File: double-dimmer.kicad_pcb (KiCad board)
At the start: 2 copper layers, 91.4 x 56.6 mm, 5 parts, among them J1 Netzspannung, J2 Screw_Terminal_01x05, J3 Conn_01x04

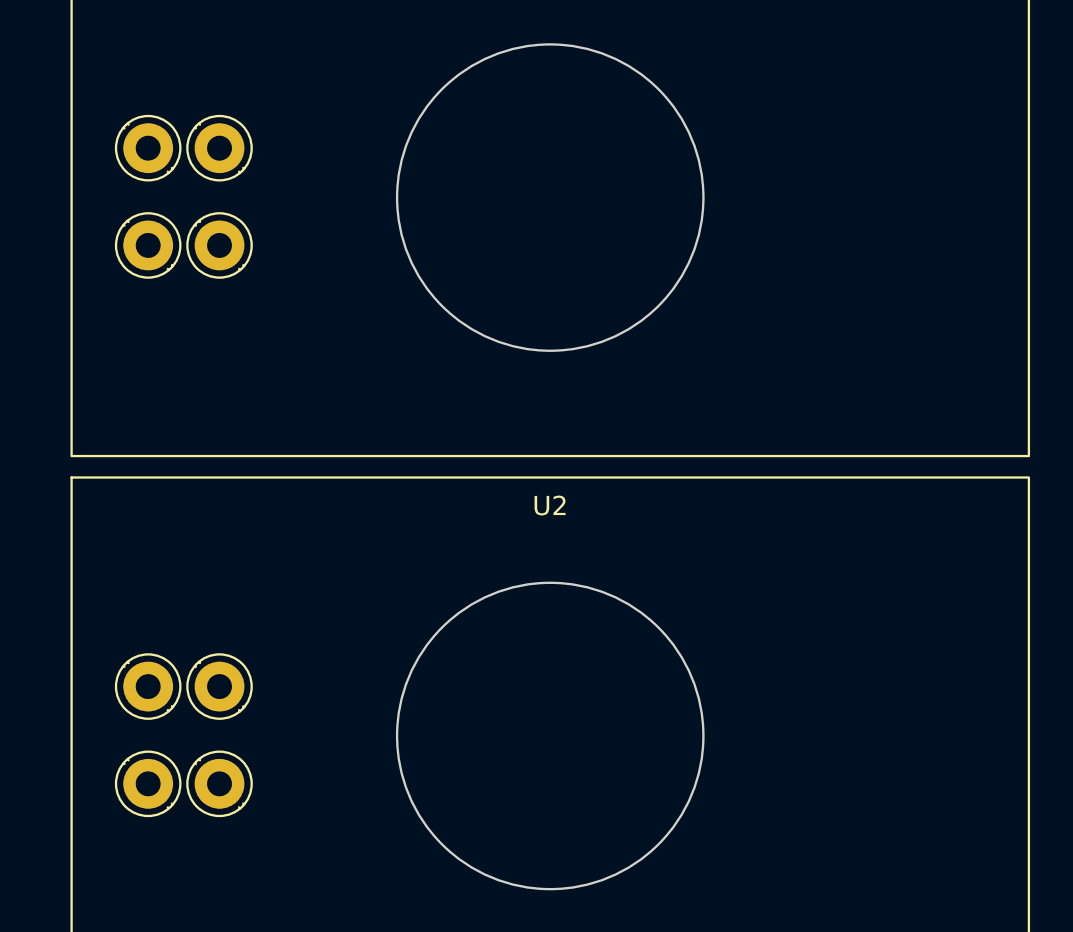
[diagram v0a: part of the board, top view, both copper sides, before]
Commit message: Update dimmer footprint and add fuse and a switch
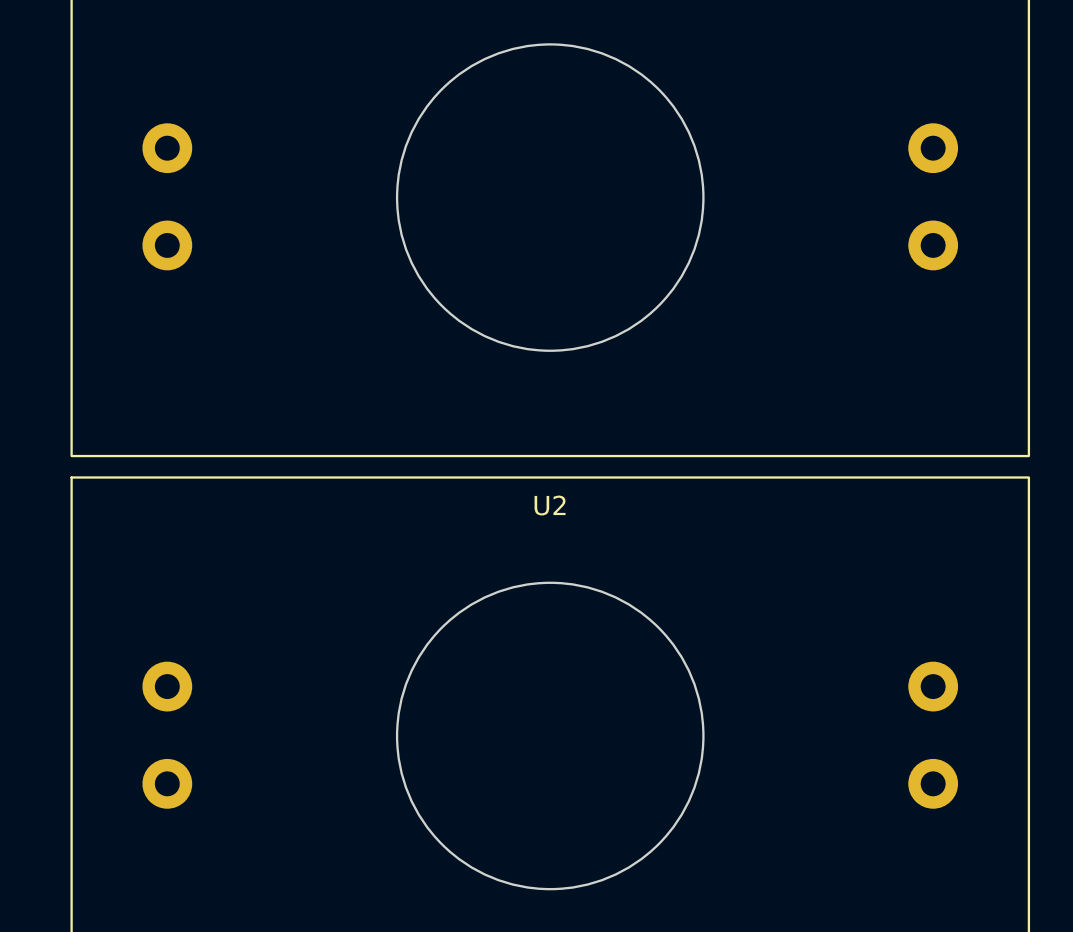
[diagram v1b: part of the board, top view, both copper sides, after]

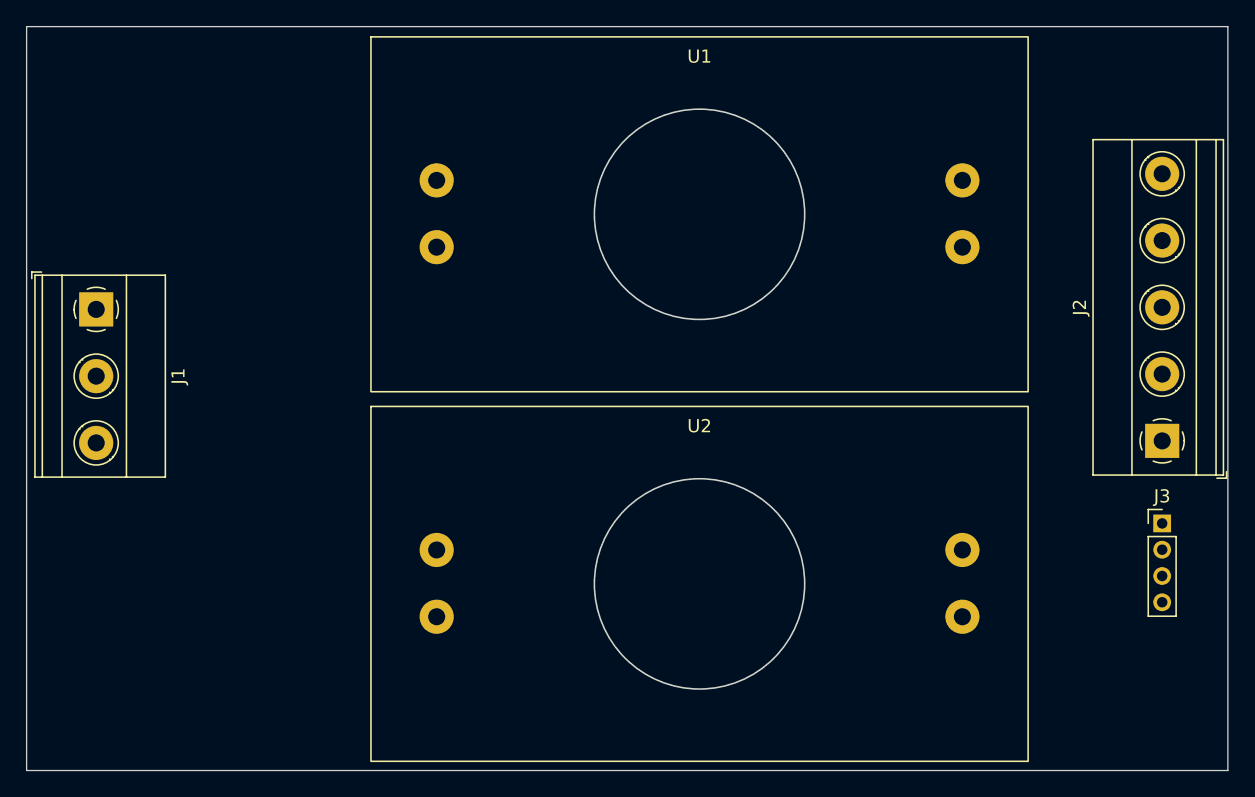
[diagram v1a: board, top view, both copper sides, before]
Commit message: Update dimmer footprint and symbol
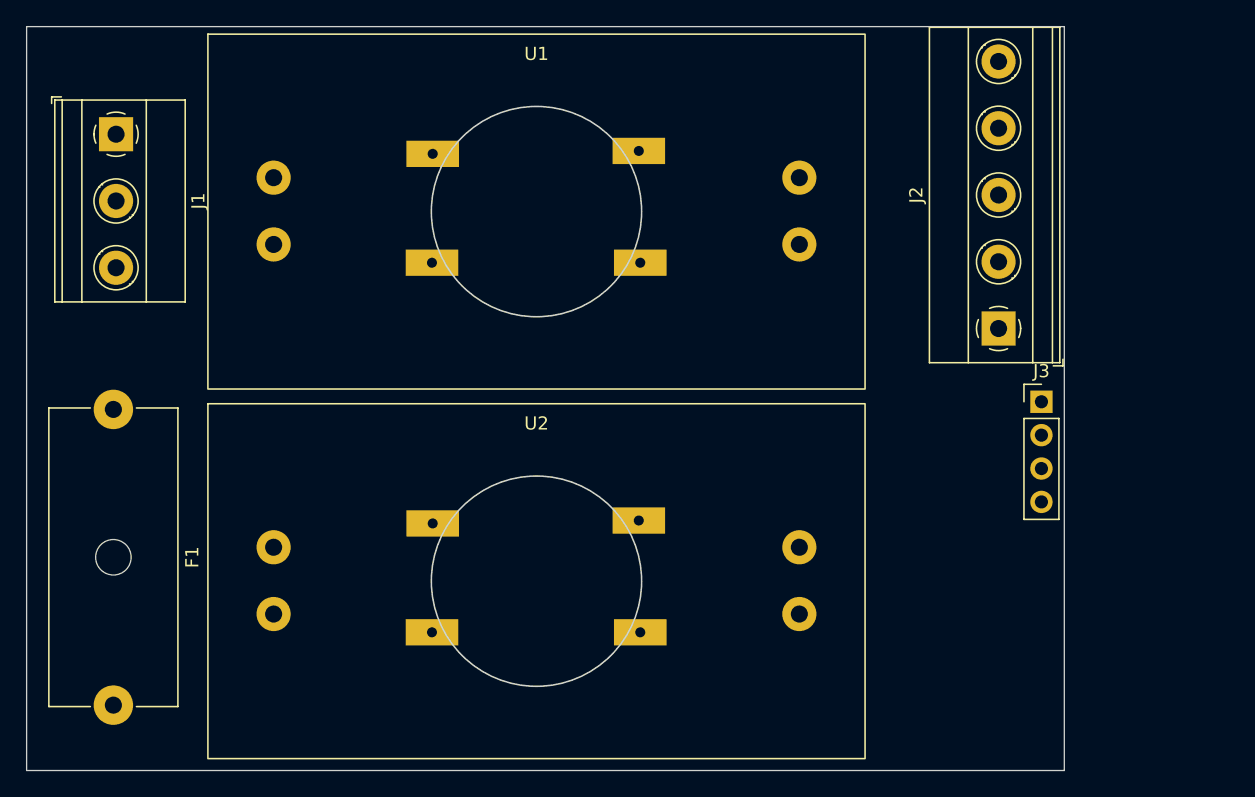
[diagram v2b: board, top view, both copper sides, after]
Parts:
- added F1: Fuse, Fuse:Fuseholder_Cylinder-5x20mm_Schurter_0031_8201_Horizontal_Open, F.Cu at (66.8, 83.9)
- J3: footprint Connector_PinHeader_2.00mm:PinHeader_1x04_P2.00mm_Vertical -> Connector_PinHeader_2.54mm:PinHeader_1x04_P2.54mm_Vertical
- moved J2 15.1 mm to (134.2, 77.8)
- moved J1 13.4 mm to (67.0, 63.0)
- moved J3 13.0 mm to (137.4, 83.3)
- moved U1 12.4 mm to (99.0, 68.9)
- moved U2 12.4 mm to (99.0, 97.0)
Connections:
- J1 pad 1: N -> Earth
- J1 pad 2: Earth -> N
- J1 pad 3: L -> Net-(J1-Pin_3)
- U1 pad 1: (no net) -> L
- U1 pad 2: (no net) -> N
- U1 pad 3: (no net) -> Net-(J2-Pin_5)
- U1 pad 4: (no net) -> Net-(J2-Pin_4)
- U2 pad 1: (no net) -> L
- U2 pad 2: (no net) -> N
- U2 pad 3: (no net) -> Net-(J2-Pin_3)
- U2 pad 4: (no net) -> Net-(J2-Pin_2)
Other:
- board size 91.4 x 56.6 mm -> 79 x 56.6 mm

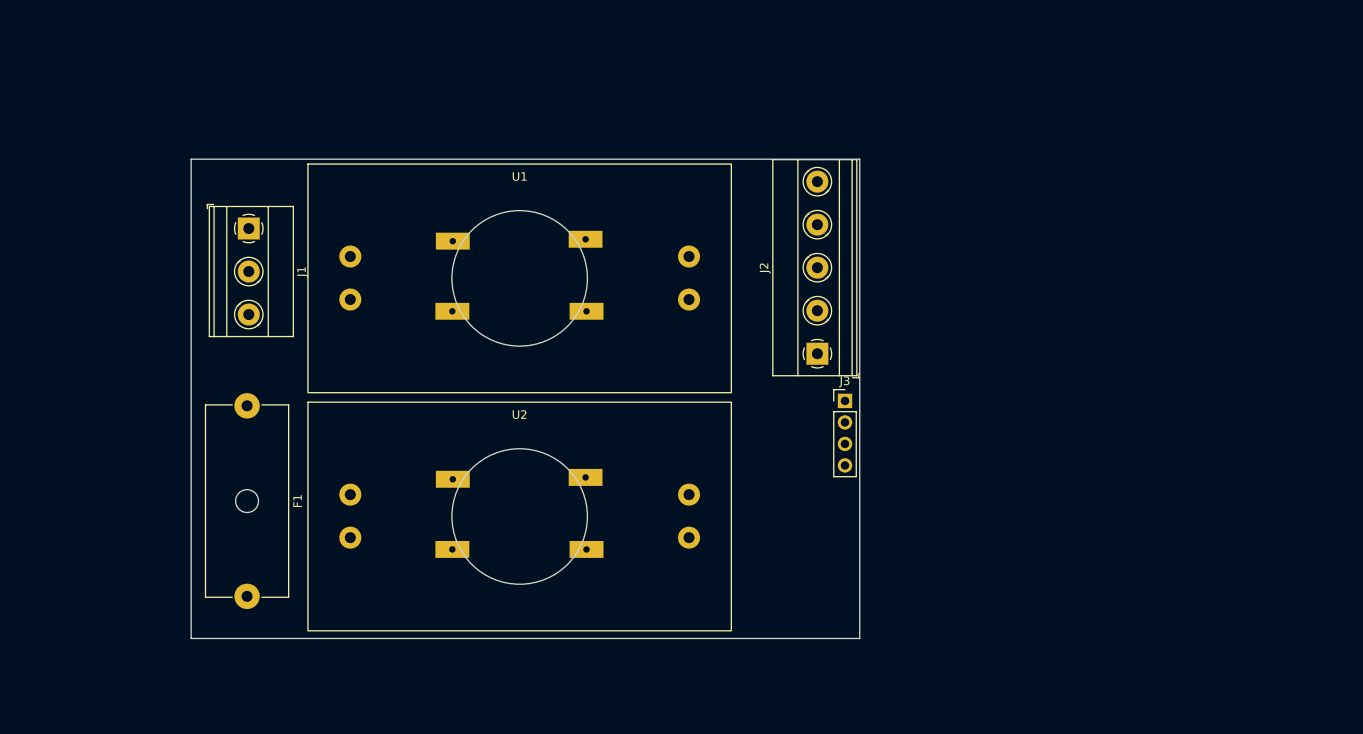
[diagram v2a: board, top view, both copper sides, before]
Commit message: Added switches to layout and do routing
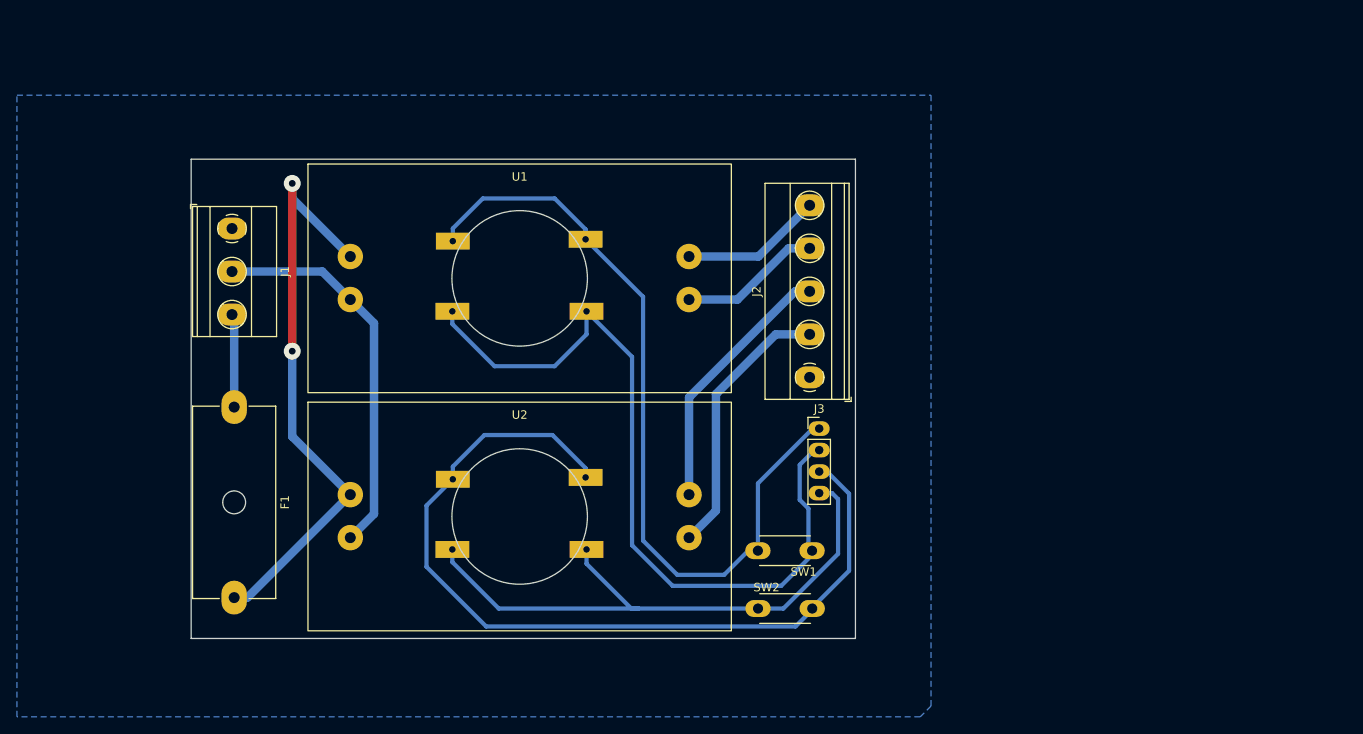
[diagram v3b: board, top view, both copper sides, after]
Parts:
- added SW1: SW_Push, pts636:pts636, F.Cu at (133.5, 101.0)
- added SW2: SW_Push, pts636:pts636, F.Cu at (127.1, 107.9)
- moved J3 4.47 mm to (134.4, 86.6)
- moved J2 2.94 mm to (133.2, 80.6)
- moved J1 1.98 mm to (65.0, 63.0)
- moved F1 1.53 mm to (65.3, 84.1)
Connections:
- net Net-(J1-Pin_3) renamed L_Prefuse
- net Net-(J2-Pin_2) renamed N_OUT2
- net Net-(J2-Pin_3) renamed L_OUT2
- net Net-(J2-Pin_4) renamed N_OUT1
- net Net-(J2-Pin_5) renamed L_OUT1
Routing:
- net Switch_A2: track 0.00 -> 102.5 mm
- net Switch_A1: track 0.00 -> 94.0 mm
- net Switch_B1: track 0.00 -> 92.6 mm
- net Switch_B2: track 0.00 -> 71.0 mm
- net L: track 0.00 -> 69.8 mm, vias 0 -> 2
- net N: track 0.00 -> 45.8 mm
- net N_OUT2: track 0.00 -> 32.3 mm
- net L_OUT2: track 0.00 -> 30.9 mm
- net N_OUT1: track 0.00 -> 16.7 mm
- net L_OUT1: track 0.00 -> 16.7 mm
- net L_Prefuse: track 0.00 -> 11.0 mm
- added copper zone on B.Cu, net Earth
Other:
- board size 79 x 56.6 mm -> 78.4 x 56.6 mm

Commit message: Properly label the dimmers terminals
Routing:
- net (no net): track 0.00 -> 266.1 mm
- net L: track 69.8 -> 52.4 mm, vias 2 -> 0
- net N_OUT2: track 32.3 -> 40.3 mm
- net Switch_A1: track 94.0 -> 99.5 mm
- net L_OUT2: track 30.9 -> 35.9 mm
- net Switch_B1: track 92.6 -> 97.0 mm
- net Switch_B2: track 71.0 -> 70.0 mm
- net N: track 45.8 -> 45.3 mm, vias 0 -> 2

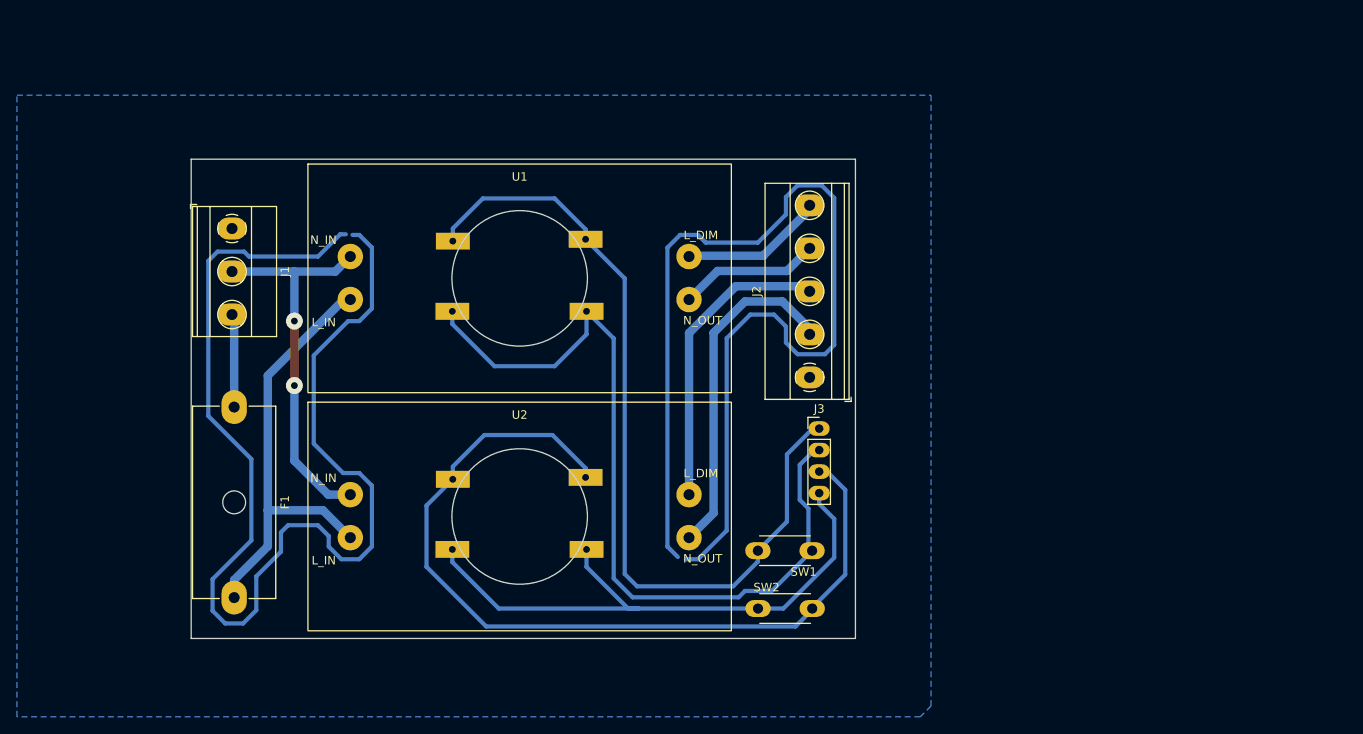
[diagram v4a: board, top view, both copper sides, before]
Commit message: Add mounting holes
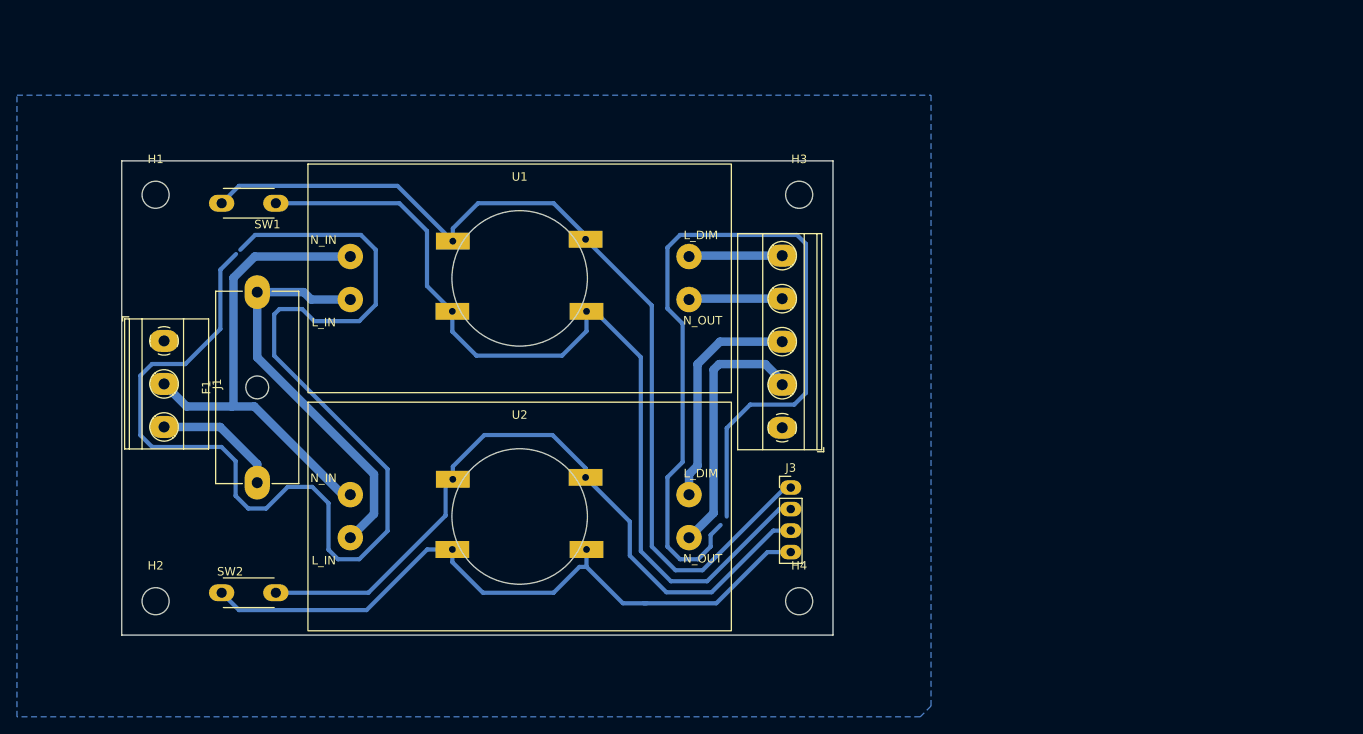
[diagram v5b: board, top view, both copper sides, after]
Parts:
- added H1: MountingHole, MountingHole:MountingHole_3.2mm_M3, F.Cu at (56.0, 59.0)
- added H2: MountingHole, MountingHole:MountingHole_3.2mm_M3, F.Cu at (56.0, 107.0)
- added H3: MountingHole, MountingHole:MountingHole_3.2mm_M3, F.Cu at (132.0, 59.0)
- added H4: MountingHole, MountingHole:MountingHole_3.2mm_M3, F.Cu at (132.0, 107.0)
- moved SW1 75.5 mm to (70.2, 60.0)
- moved SW2 63.4 mm to (63.8, 106.0)
- moved J1 15.5 mm to (57.0, 76.3)
- moved F1 9.33 mm to (68.0, 93.0), turned to 90 degrees
- moved J3 7.73 mm to (131.0, 93.6)
- moved J2 6.77 mm to (130.0, 86.5)
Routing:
- net (no net): track 266.1 -> 244.2 mm
- net Switch_A2: track 102.1 -> 85.1 mm
- net Switch_A1: track 99.5 -> 112.5 mm
- net N: track 45.3 -> 57.5 mm, vias 2 -> 0
- net Switch_B2: track 70.0 -> 82.0 mm
- net Switch_B1: track 97.0 -> 107.2 mm
- net N_OUT2: track 40.3 -> 30.7 mm
- net L_OUT2: track 35.9 -> 26.9 mm
- net L_OUT1: track 17.0 -> 11.0 mm
- net N_OUT1: track 16.7 -> 11.0 mm
- net L: track 52.4 -> 47.2 mm
- net L_Prefuse: track 11.0 -> 15.0 mm
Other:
- board size 78.4 x 56.6 mm -> 84 x 56 mm
